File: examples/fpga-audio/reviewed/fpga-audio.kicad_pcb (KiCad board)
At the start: 2 copper layers, 100 x 84 mm, 29 parts, among them J1 3V3 IN, J2 AUDIO OUT, J3 SPI PROG, U1 iCE40UP5K, U2 PCM5102A, U3 AP2112K-1.2, U4 W25Q32JV, X1 12MHz

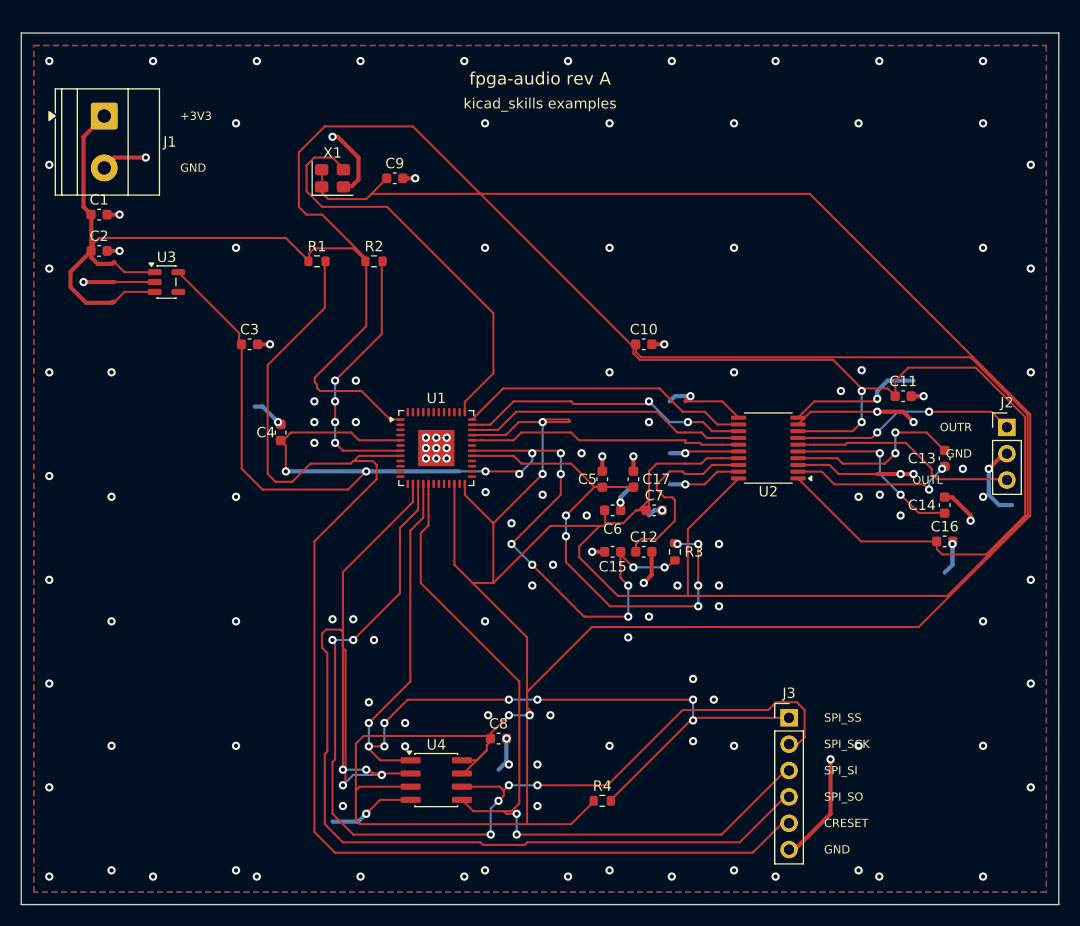
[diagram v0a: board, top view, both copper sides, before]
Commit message: Measure the fold itself, spread it, and keep stitch vias on the board
The reviewer's correction to round thirteen: the circled motor corners
were the bends, not the pour. route.hairpin measures the pair - two
same-direction corners within 1.2 mm summing past 100 degrees, arms of
0.8 mm or more so a via-skirting bump does not count, staircases
cancelling by sign; six findings across the 18 demo projects, info,
promoted only for generated boards. _spread_hairpins answers it by
stretching the fold's middle to 1.2 mm and re-doglegging onto the far
end of the outgoing straight. And stitch-via candidates now stay inside
the pour: offset from a track end, two landed past it - one dead on the
outline - as an edge violation and an orphan at once.

Four boards pass their gates with zero hairpins; the FPGA board's fresh
route is still being drawn.

Co-Authored-By: Claude Fable 5 <noreply@anthropic.com>
Claude-Session: https://claude.ai/code/session_01DUj7Ltu92tWg159mCSacwY
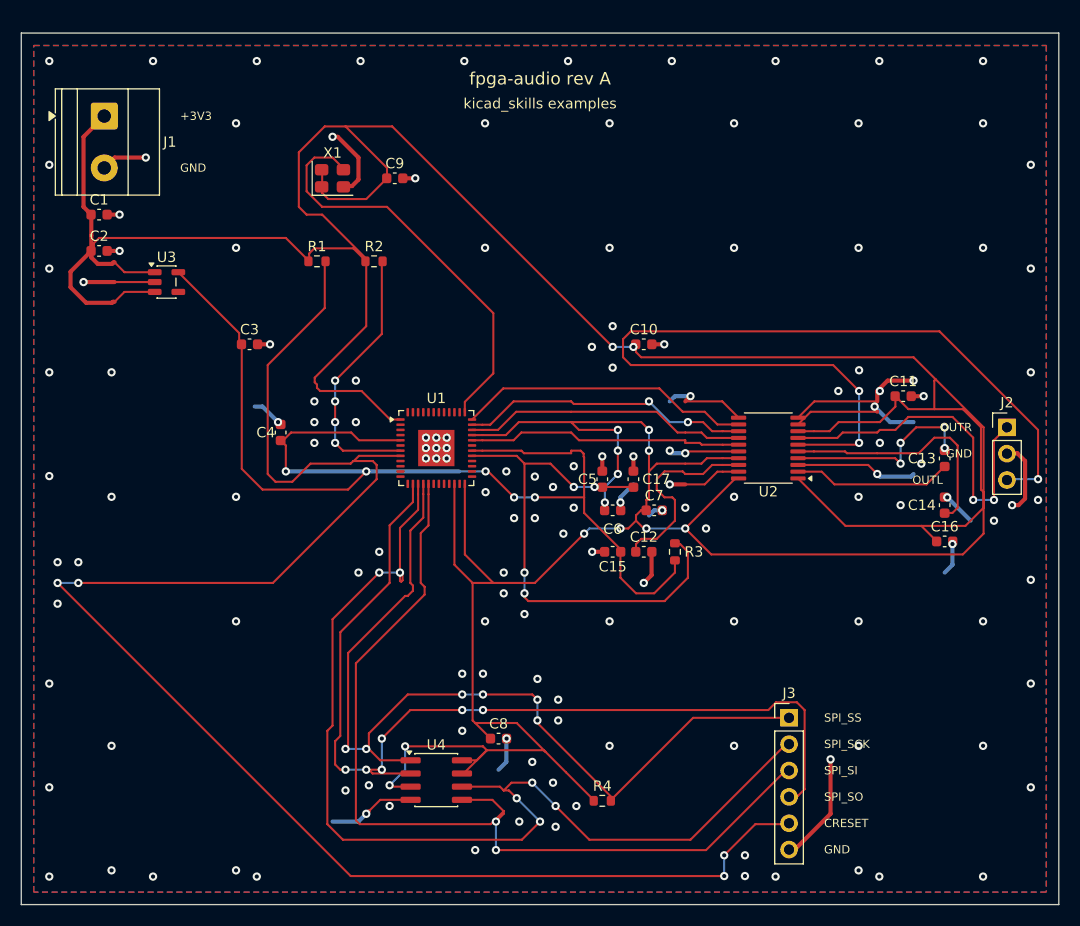
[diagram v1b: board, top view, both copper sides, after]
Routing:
- net +3V3: track 670.7 -> 455.3 mm, vias 6 -> 14
- net /OUTL: track 22.0 -> 88.8 mm, vias 0 -> 3
- net /CRESET: track 124.9 -> 161.1 mm, vias 0 -> 4
- net /SPI_SO: track 126.1 -> 94.0 mm, vias 4 -> 6
- net /SPI_SI: track 73.6 -> 90.6 mm
- net /OUTR: track 21.8 -> 34.1 mm
- net /+1V2: track 121.9 -> 112.7 mm, vias 13 -> 5
- net /VNEG: track 17.8 -> 23.9 mm, vias 2 -> 0
- net /SPI_SCK: track 98.9 -> 104.4 mm
- net /VCCPLL: track 48.0 -> 50.6 mm, vias 6 -> 4
- net /CAPM: track 17.5 -> 19.2 mm, vias 2 -> 4
- net /SPI_SS: track 89.5 -> 88.3 mm, vias 8 -> 6
- net /CAPP: track 16.2 -> 15.4 mm, vias 2 -> 0
- net GND: track 137.1 -> 137.8 mm, vias 145 -> 149

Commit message: Regenerate the five on the arc and the restored pour, and write it down
The FPGA board's fresh route reproduced its round-fourteen debt to the
digit - after three independent cold draws that is the floorplan fact the
gate says it is, not luck. All five boards measure zero hairpins, zero
crossings, zero doubled runs; the four fast boards pass their gates.
REVIEW.md section 20 records the arc, the retraction of the tongue
pruning, and where the FPGA board stands.

Co-Authored-By: Claude Fable 5 <noreply@anthropic.com>
Claude-Session: https://claude.ai/code/session_01DUj7Ltu92tWg159mCSacwY
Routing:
- net GND: vias 149 -> 148
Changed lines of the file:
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@@
 	(segment (start 148.45 100.5) (end 153.0 100.5) (width 0.2) (layer "F.Cu") (net 2))
 	(segment (start 153.0 100.5) (end 153.0 100.25) (width 0.2) (layer "F.Cu") (net 2))
-	(segment (start 153.0 100.25) (end 153.913 100.25) (width 0.2) (layer "F.Cu") (net 2))
-	(segment (start 153.913 100.25) (end 154.2 100.538) (width 0.2) (layer "F.Cu") (net 2))
-	(segment (start 154.2 100.538) (end 154.2 100.825) (width 0.2) (layer "F.Cu") (net 2))
-	(segment (start 154.2 100.825) (end 154.25 100.875) (width 0.2) (layer "F.Cu") (net 2))
+	(segment (start 153.0 100.25) (end 154.2 100.25) (width 0.2) (layer "F.Cu") (net 2))
+	(segment (start 154.2 100.25) (end 154.25 100.3) (width 0.2) (layer "F.Cu") (net 2))
+	(segment (start 154.25 100.3) (end 154.25 100.875) (width 0.2) (layer "F.Cu") (net 2))
 	(segment (start 154.25 100.875) (end 154.25 104.75) (width 0.2) (layer "F.Cu") (net 2))
 	(segment (start 143.45 100.75) (end 147.75 100.75) (width 0.2) (layer "F.Cu") (net 20))
@@
 	(via (at 120.7 140.7) (size 0.8) (drill 0.4) (layers "F.Cu" "B.Cu") (net 1))
 	(via (at 180.7 140.7) (size 0.8) (drill 0.4) (layers "F.Cu" "B.Cu") (net 1))
-	(via (at 184.75 105.5) (size 0.8) (drill 0.4) (layers "F.Cu" "B.Cu") (net 1))
 	(zone
 		(net 1)

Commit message: Start the turn at the head of the leg, with no stub at all
The reviewer's last correction on the reversal: the bend back to nine
o'clock - the lead stub the arc kept out the old heading - is not part
of the ideal figure. The turn now starts right where the incoming
straight begins, where the escape's own 45 already points the line, so
the trace draws one continuous curve from pad to bus. Two changes make
that fit: lead 0 is tried before any stub, and when the exit leg is too
short to land on without overshooting, the turn carries through the
exit's own 45 and lands on the straight beyond it.

The motor board's two reversals regenerate as equal-legged turns with
no stub; the FPGA board re-routes (the cache was lost to a container
reclaim) and reproduces its documented debt to the digit for a fourth
independent draw. The as-generated gate counts in the examples README
had drifted behind the rule set and are refreshed while the numbers
were being re-measured.

Co-Authored-By: Claude Fable 5 <noreply@anthropic.com>
Claude-Session: https://claude.ai/code/session_01DUj7Ltu92tWg159mCSacwY
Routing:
- net /+1V2: track 112.9 -> 112.2 mm
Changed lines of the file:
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@@
 	(segment (start 148.2 100.25) (end 148.45 100.5) (width 0.2) (layer "F.Cu") (net 2))
 	(segment (start 148.45 100.5) (end 153.0 100.5) (width 0.2) (layer "F.Cu") (net 2))
-	(segment (start 153.0 100.5) (end 153.0 100.25) (width 0.2) (layer "F.Cu") (net 2))
-	(segment (start 153.0 100.25) (end 154.2 100.25) (width 0.2) (layer "F.Cu") (net 2))
-	(segment (start 154.2 100.25) (end 154.25 100.3) (width 0.2) (layer "F.Cu") (net 2))
-	(segment (start 154.25 100.3) (end 154.25 100.875) (width 0.2) (layer "F.Cu") (net 2))
+	(segment (start 153.0 100.5) (end 153.875 100.5) (width 0.2) (layer "F.Cu") (net 2))
+	(segment (start 153.875 100.5) (end 154.25 100.875) (width 0.2) (layer "F.Cu") (net 2))
 	(segment (start 154.25 100.875) (end 154.25 104.75) (width 0.2) (layer "F.Cu") (net 2))
 	(segment (start 143.45 100.75) (end 147.75 100.75) (width 0.2) (layer "F.Cu") (net 20))

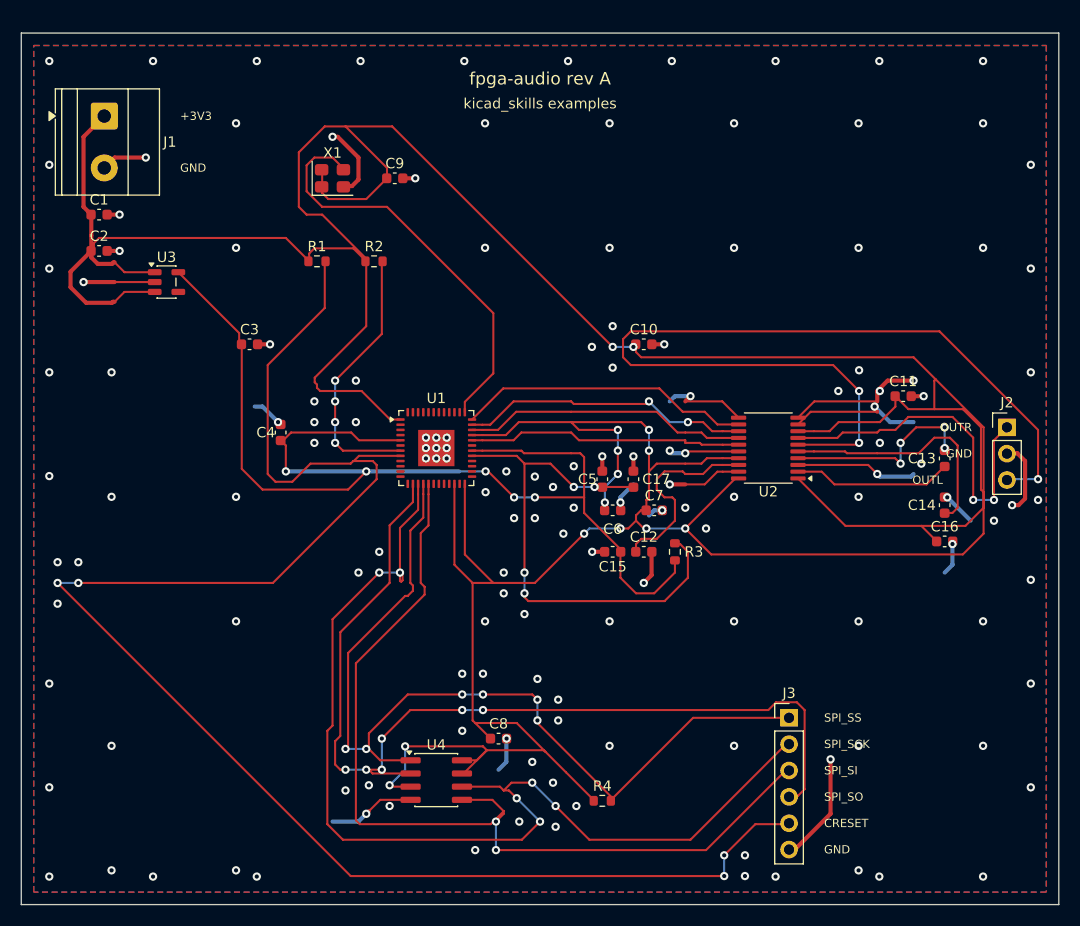
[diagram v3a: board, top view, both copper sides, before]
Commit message: Move the parts out of the corridor, and the tour goes with them
The FPGA board routes again, and better than it did. Letting one track
be promoted more than once before the loop calls its lane impossible was
the last piece: every net that failed had routed on its own when asked,
which is an order to be found rather than a floorplan with none.

Moving the seven parts out from between the two escape fans paid a debt
three rounds old. The line-out tour - 88 mm of copper for a 20 mm net,
`route.detour` and `route.wander` both naming it, reproduced across four
independent cold draws and written down each time as floorplan rather
than routing - is gone; both rules now report nothing. The board's gate
goes from four blocking findings to two, and what is left is the
two-layer bill it has always been: three SPI nets crossing cuts in the
plane, three corners.

Across the five boards: no via sits in a land, DRC is clean on both
matrix versions, and every board keeps zero hairpins, zero crossings and
zero mid-run width steps. The example README's verdict rows are
re-measured, and the guides and REVIEW carry what the ban cost and what
buying it back taught.

Co-Authored-By: Claude Fable 5 <noreply@anthropic.com>
Claude-Session: https://claude.ai/code/session_01DUj7Ltu92tWg159mCSacwY
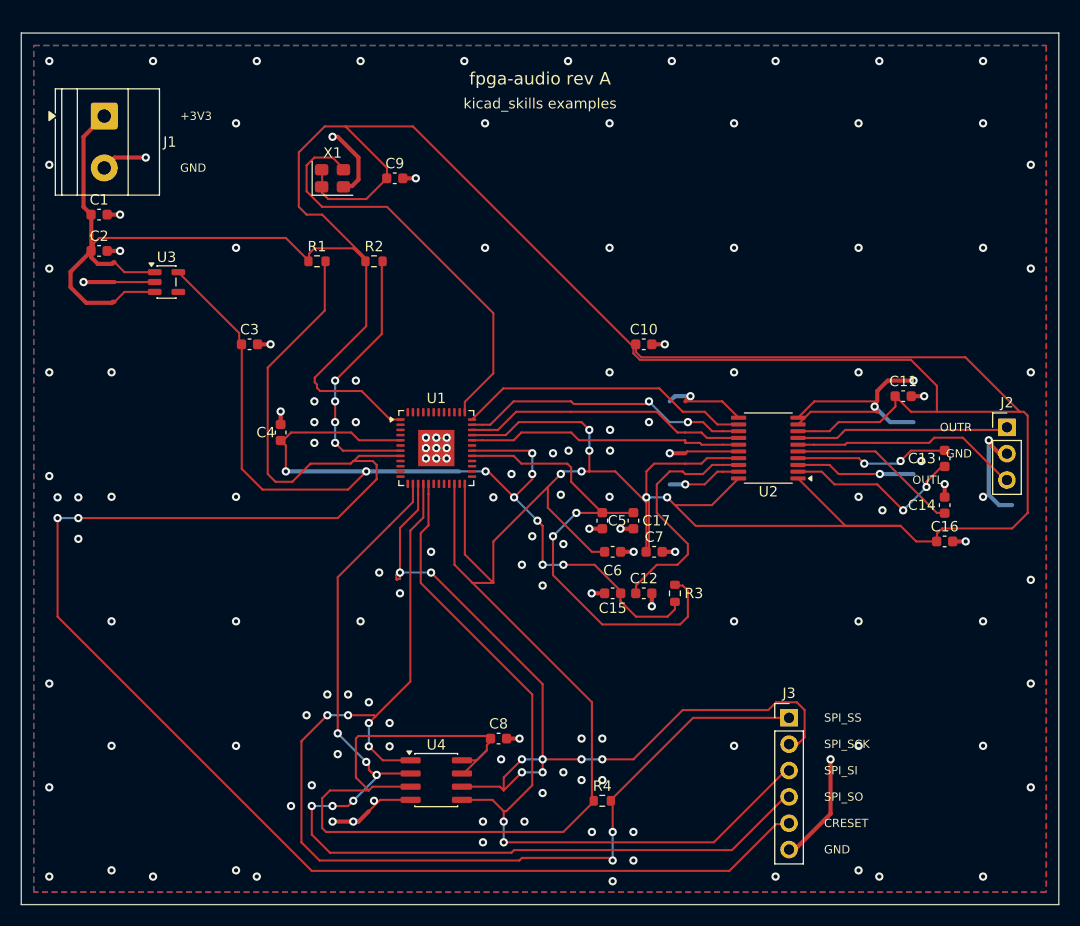
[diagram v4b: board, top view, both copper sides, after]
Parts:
- moved C12 4.00 mm to (160.0, 114.0)
- moved C15 4.00 mm to (157.0, 114.0)
- moved C17 4.00 mm to (159.0, 107.0), turned to 270 degrees
- moved C5 4.00 mm to (156.0, 107.0), turned to 270 degrees
- moved C6 4.00 mm to (157.0, 110.0)
- moved C7 4.00 mm to (161.0, 110.0)
- moved R3 4.00 mm to (163.0, 114.0)
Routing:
- net /OUTL: track 88.8 -> 22.1 mm, vias 3 -> 0
- net +3V3: track 455.3 -> 513.4 mm, vias 14 -> 6
- net /SPI_SCK: track 104.4 -> 84.5 mm, vias 6 -> 8
- net /SPI_SS: track 88.3 -> 107.5 mm
- net /SPI_SI: track 90.6 -> 75.5 mm
- net /OUTR: track 34.1 -> 20.6 mm, vias 2 -> 0
- net GND: track 137.8 -> 128.3 mm, vias 148 -> 150
- net /VNEG: track 23.9 -> 16.6 mm
- net /LDOO: track 19.3 -> 23.9 mm
- net /CAPM: track 19.2 -> 14.9 mm, vias 4 -> 2
- net /CRESET: track 161.1 -> 165.0 mm, vias 4 -> 2
- net /+1V2: track 112.2 -> 108.4 mm, vias 5 -> 9
- net /VCCPLL: track 50.6 -> 47.6 mm, vias 4 -> 2
- net /SPI_SO: track 94.0 -> 96.4 mm
- net /CAPP: track 15.4 -> 17.7 mm, vias 0 -> 2

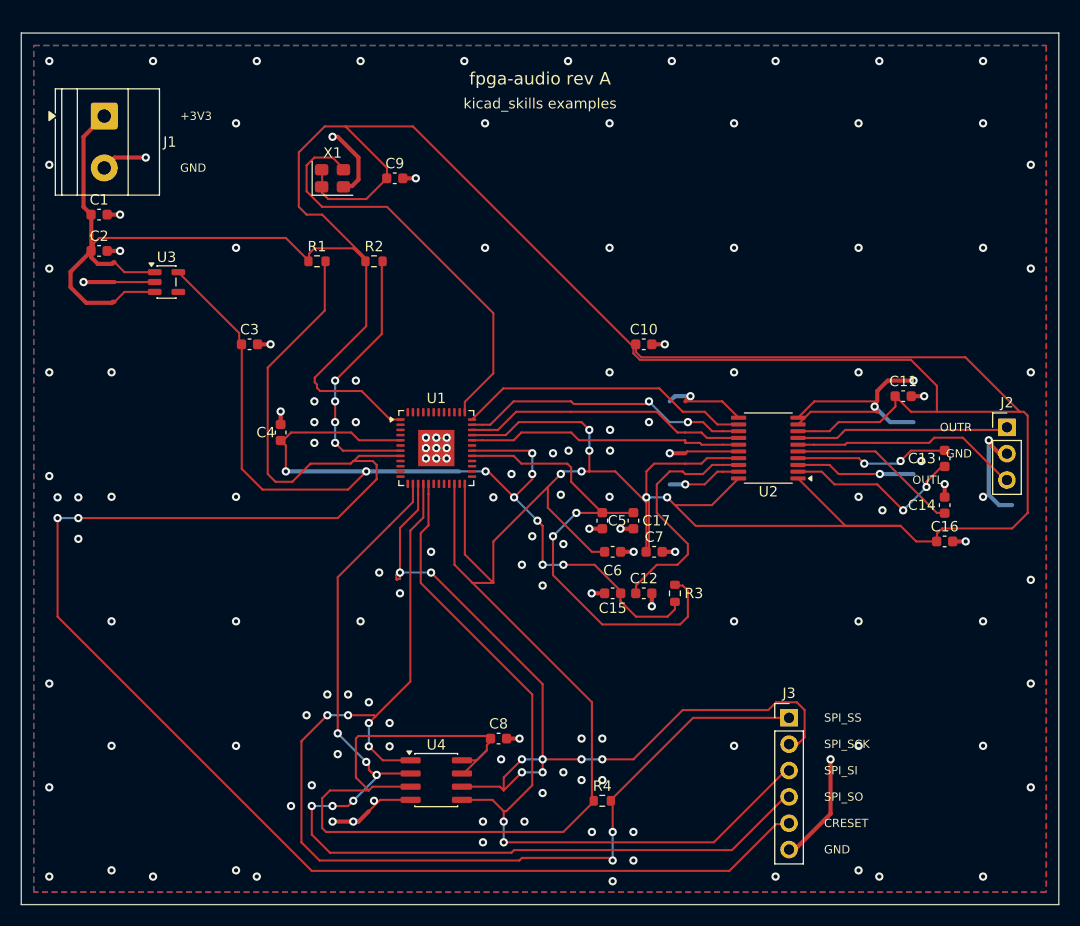
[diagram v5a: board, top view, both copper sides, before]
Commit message: Relieve the pads, fillet the joints, and give the board its screw holes
Three of the reviewer's manufacturing points, and they largely fall out
of the one before it - once KiCad fills the plane, the thermal relief it
was already asked for in the file actually appears.

**Thermal relief.** The zones said thermal all along; our own filler
ignored it and flooded every land solid. KiCad's does not, so every
through-hole ground pad now sits in a gap bridged by four spokes and an
iron can bring the joint up without heating a hundred square millimetres
of copper. `layout.solid_pad_connection` reports the setting when a
board turns it off: drilled pads only, because a surface pad reflows in
an oven that is heating the plane anyway and flooding it is often the
better thermal answer.

**Teardrops.** A track entering a land is a step change in width, and a
step change is where copper tears - the connector gets levered on and
off, the drill wanders, and the crack starts at the corner. `_teardrops`
replaces the first stretch of each run with a three-step taper into the
land, checked against its neighbours before it is kept, so a fillet
never eats the clearance a fine-pitch escape needs. It *replaces* rather
than overlays: laying the taper on top of the run drew the same copper
twice, and `route.acute_angle` reported all thirty of them, correctly.
`route.mixed_track_widths` learns what a fillet looks like so a properly
filleted board does not read as one nobody decided the width of.

**Mounting holes.** Four M3 holes near the corners, placed before the
router runs because they are obstacles, and slid along the edges or a
little inboard where a connector body has the corner - the motor board
and the op-amp take three, which is what those floorplans have room for.
Grounded on the motor driver, whose chassis is metal and part of the
shield, plain on the rest: bonding the enclosure to the reference is the
enclosure's decision, not the board's.

Two things that fell out of placing par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
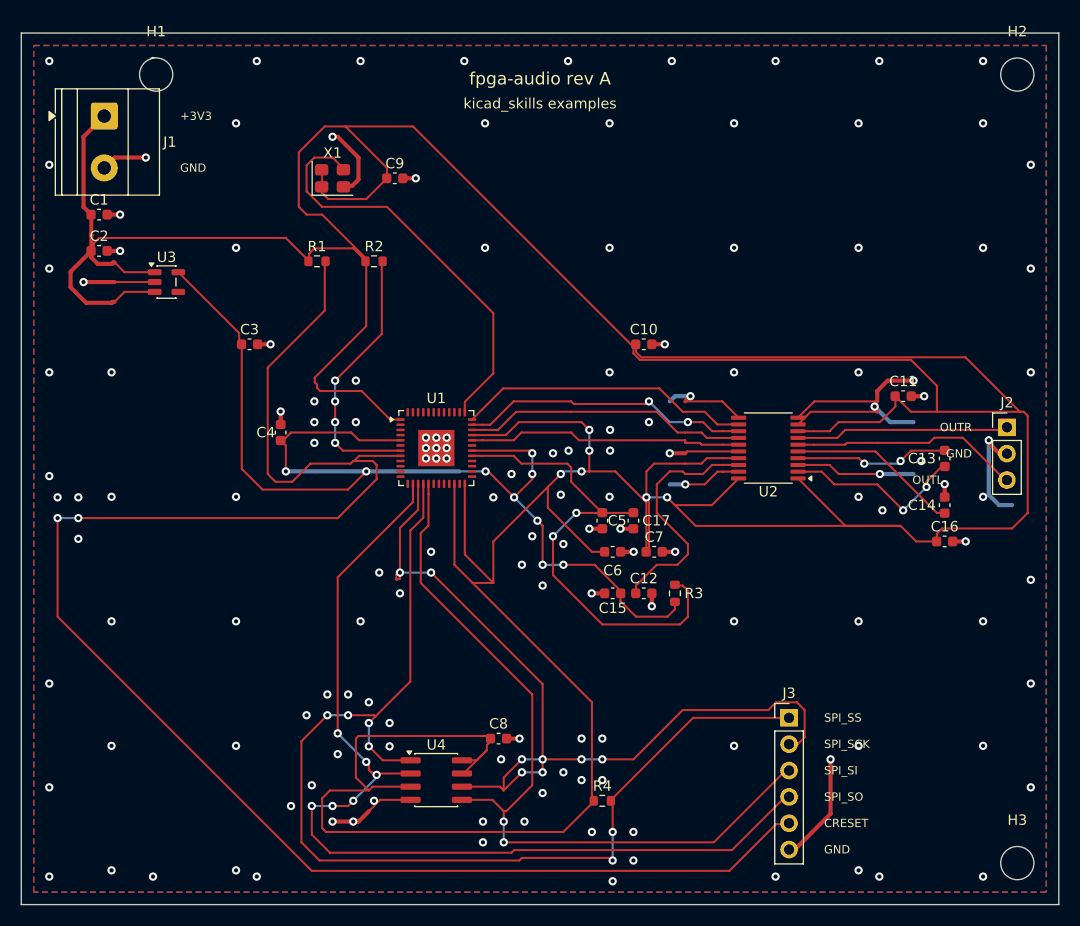
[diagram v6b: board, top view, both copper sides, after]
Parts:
- added H1: M33, MountingHole:MountingHole_3.2mm_M3, F.Cu at (113.0, 64.0)
- added H2: M33, MountingHole:MountingHole_3.2mm_M3, F.Cu at (196.0, 64.0)
- added H3: M33, MountingHole:MountingHole_3.2mm_M3, F.Cu at (196.0, 140.0)
